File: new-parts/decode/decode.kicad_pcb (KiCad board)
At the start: 2 copper layers, 96.5 x 82.5 mm, 45 parts, among them J1 BHR-10-VUA, J10 Conn_02x01, J11 Conn_02x01, J12 Conn_02x01, J13 Conn_02x01, J14 Conn_02x01, J2 Conn_02x01, J3 Conn_02x01, J4 Conn_02x01, J5 Conn_02x01, J6 Conn_02x03_Odd_Even, J7 Conn_02x01, J8 Conn_02x01, J9 Conn_02x01, K1 J104D2C12VDC.15S, K2 J104D2C12VDC.15S, K3 J104D2C12VDC.15S, K4 J104D2C12VDC.15S, K5 J104D2C12VDC.15S, K6 J104D2C12VDC.15S, K7 J104D2C12VDC.15S, K8 J104D2C12VDC.15S, K9 J104D2C12VDC.15S

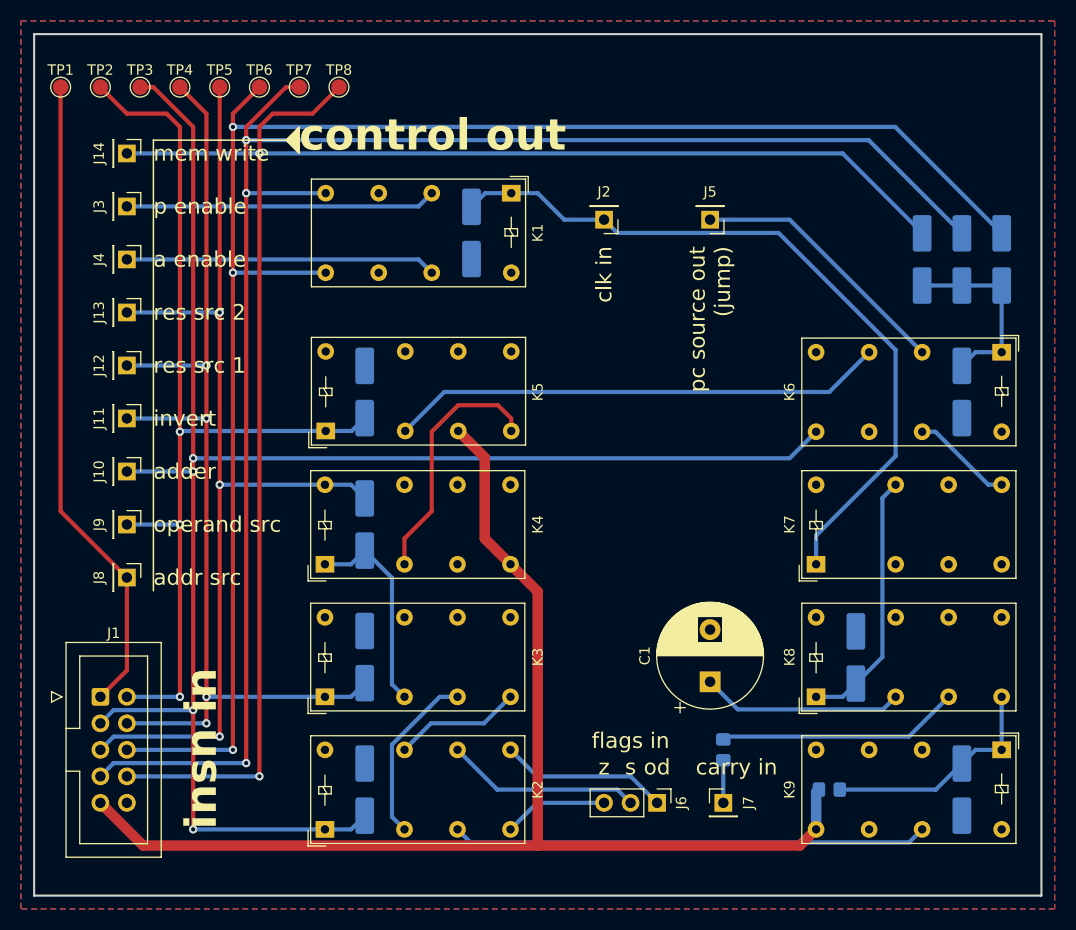
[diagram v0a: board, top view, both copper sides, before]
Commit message: decode: Also provide !invert control signal as carry in for the adder, provide 4 pins for every control signal.
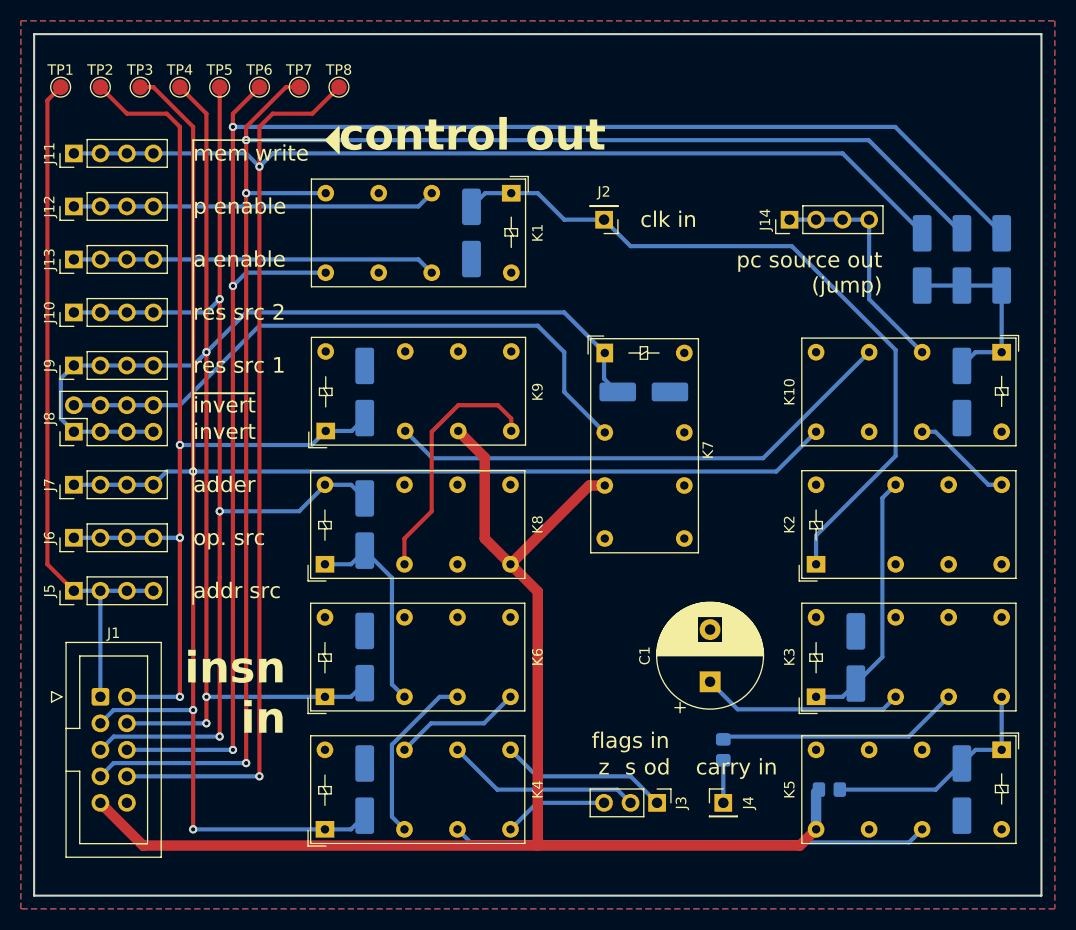
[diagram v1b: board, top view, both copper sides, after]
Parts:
- removed the J3 at (142.2, 43.2)
- removed the J4 at (142.2, 48.3)
- added D6: SMAJ14CA, Diode_SMD:D_SMA_Handsoldering, B.Cu at (191.8, 61.0)
- added J6: Conn_01x04, Connector_PinHeader_2.54mm:PinHeader_1x04_P2.54mm_Vertical, F.Cu at (137.2, 74.9)
- added J7: Conn_01x04, Connector_PinHeader_2.54mm:PinHeader_1x04_P2.54mm_Vertical, F.Cu at (137.2, 69.8)
- added K7: J104D2C12VDC.15S, Relay_THT:Relay_DPDT_Finder_30.22, F.Cu at (188.0, 57.2)
- J10, J11, J12, J13, J14, J5, J9: value Conn_02x01 -> Conn_01x04; footprint Connector_PinHeader_2.54mm:PinHeader_1x01_P2.54mm_Vertical -> Connector_PinHeader_2.54mm:PinHeader_1x04_P2.54mm_Vertical
- J2: value Conn_02x01 -> Conn_01x01
- J3: renamed from J6; value Conn_02x03_Odd_Even -> Conn_01x03
- J4: renamed from J7; value Conn_02x01 -> Conn_01x01
- J8: value Conn_02x01 -> Conn_02x04_Odd_Even; footprint Connector_PinHeader_2.54mm:PinHeader_1x01_P2.54mm_Vertical -> Connector_PinHeader_2.54mm:PinHeader_2x04_P2.54mm_Vertical
- moved J5 70.6 mm to (137.2, 80.0), turned to 90 degrees
- moved J14 63.8 mm to (205.7, 44.5), turned to 90 degrees
- moved J11 25.9 mm to (137.2, 38.1), turned to 90 degrees
- moved J12 16.1 mm to (137.2, 43.2), turned to 90 degrees
- moved J10 16.1 mm to (137.2, 53.3), turned to 90 degrees
- moved J9 16.1 mm to (137.2, 58.4), turned to 90 degrees
- moved J8 14.9 mm to (137.2, 64.8), turned to 90 degrees
- moved J13 7.18 mm to (137.2, 48.3), turned to 90 degrees
- renumbered D8 to D10, D9 to D11, D6 to D12, D11 to D2, D2 to D3, D12 to D4, D3 to D5, D4 to D7, D5 to D8, D7 to D9, K6 to K10, K7 to K2, K8 to K3, K2 to K4, K9 to K5, K3 to K6, K4 to K8, K5 to K9
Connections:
- J10 pad 1: add -> cinv
- J11 pad 1: c2 -> m en
- J12 pad 1: c2 -> /p en out
- J13 pad 1: cinv -> /a en out
- J14 pad 1: m en -> /pc src out
- J5 pad 1: /pc src out -> as
- J8 pad 1: as -> c2
- J9 pad 1: cond -> c2
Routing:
- net ~{inv}: track 0.00 -> 60.5 mm
- net c2: track 100.6 -> 159.3 mm, vias 4 -> 3
- net VCC: track 117.7 -> 129.9 mm
- net cinv: track 97.5 -> 104.2 mm
- net m en: track 163.5 -> 169.7 mm
- net add: track 167.5 -> 173.6 mm, vias 4 -> 3
- net cond: track 92.2 -> 97.8 mm
- net as: track 62.1 -> 67.6 mm
- net /p en out: track 29.7 -> 34.8 mm
- net /a en out: track 29.7 -> 34.8 mm
- net /pc src out: track 25.6 -> 22.4 mm
- net Net-(K10-Pad12): track 47.6 -> 49.7 mm
- net a en: track 161.5 -> 162.0 mm
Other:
- board text added: "op. src"
- board text added: "~{invert}"
- board text removed: "operand src"

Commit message: Add signatures to some boards.
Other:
- board text added: "github.com/fread/visvitalis"
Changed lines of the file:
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@@
 		(tags "Through hole pin header THT 1x04 2.54mm single row")
 		(property "Reference" "J13"
-			(at 0 -2.33 270)
+			(at 0 -2.33 -90)
 			(layer "F.SilkS")
 			(effects
@@
 		)
 		(property "Value" "Conn_01x04"
-			(at 0 9.95 270)
+			(at 0 9.95 -90)
 			(layer "F.Fab")
 			(effects
@@
 		)
 		(fp_text user "${REFERENCE}"
-			(at 0 3.81 360)
+			(at 0 3.81 0)
 			(layer "F.Fab")
 			(effects
@@
 		(tags "Through hole pin header THT 1x04 2.54mm single row")
 		(property "Reference" "J10"
-			(at 0 -2.33 270)
+			(at 0 -2.33 -90)
 			(layer "F.SilkS")
 			(effects
@@
 		)
 		(property "Value" "Conn_01x04"
-			(at 0 9.95 270)
+			(at 0 9.95 -90)
 			(layer "F.Fab")
 			(effects
@@
 		)
 		(fp_text user "${REFERENCE}"
-			(at 0 3.81 360)
+			(at 0 3.81 0)
 			(layer "F.Fab")
 			(effects
@@
 		(tags "Through hole pin header THT 1x04 2.54mm single row")
 		(property "Reference" "J5"
-			(at 0 -2.33 270)
+			(at 0 -2.33 -90)
 			(layer "F.SilkS")
 			(effects
@@
 		)
 		(property "Value" "Conn_01x04"
-			(at 0 9.95 270)
+			(at 0 9.95 -90)
 			(layer "F.Fab")
 			(effects
@@
 		)
 		(fp_text user "${REFERENCE}"
-			(at 0 3.81 360)
+			(at 0 3.81 0)
 			(layer "F.Fab")
 			(effects
@@
 		(tags "Through hole pin header THT 1x04 2.54mm single row")
 		(property "Reference" "J6"
-			(at 0 -2.33 270)
+			(at 0 -2.33 -90)
 			(layer "F.SilkS")
 			(effects
@@
 		)
 		(property "Value" "Conn_01x04"
-			(at 0 9.95 270)
+			(at 0 9.95 -90)
 			(layer "F.Fab")
 			(effects
@@
 		)
 		(fp_text user "${REFERENCE}"
-			(at 0 3.81 360)
+			(at 0 3.81 0)
 			(layer "F.Fab")
 			(effects
@@
 		(tags "Through hole pin header THT 2x04 2.54mm double row")
 		(property "Reference" "J8"
-			(at 1.27 -2.33 270)
+			(at 1.27 -2.33 -90)
 			(layer "F.SilkS")
 			(effects
@@
 		)
 		(property "Value" "Conn_02x04_Odd_Even"
-			(at 1.27 9.95 270)
+			(at 1.27 9.95 -90)
 			(layer "F.Fab")
 			(effects
@@
 		)
 		(fp_text user "${REFERENCE}"
-			(at 1.27 3.81 360)
+			(at 1.27 3.81 0)
 			(layer "F.Fab")
 			(effects
@@
 		(tags "Through hole pin header THT 1x04 2.54mm single row")
 		(property "Reference" "J7"
-			(at 0 -2.33 270)
+			(at 0 -2.33 -90)
 			(layer "F.SilkS")
 			(effects
@@
 		)
 		(property "Value" "Conn_01x04"
-			(at 0 9.95 270)
+			(at 0 9.95 -90)
 			(layer "F.Fab")
 			(effects
@@
 		)
 		(fp_text user "${REFERENCE}"
-			(at 0 3.81 360)
+			(at 0 3.81 0)
 			(layer "F.Fab")
 			(effects
@@
 		(tags "Through hole pin header THT 1x04 2.54mm single row")
 		(property "Reference" "J14"
-			(at 0 -2.33 270)
+			(at 0 -2.33 -90)
 			(layer "F.SilkS")
 			(effects
@@
 		)
 		(property "Value" "Conn_01x04"
-			(at 0 9.95 270)
+			(at 0 9.95 -90)
 			(layer "F.Fab")
 			(effects
@@
 		)
 		(fp_text user "${REFERENCE}"
-			(at 0 3.81 360)
+			(at 0 3.81 0)
 			(layer "F.Fab")
 			(effects
@@
 		(tags "Through hole pin header THT 1x04 2.54mm single row")
 		(property "Reference" "J11"
-			(at 0 -2.33 270)
+			(at 0 -2.33 -90)
 			(layer "F.SilkS")
 			(effects
@@
 		)
 		(property "Value" "Conn_01x04"
-			(at 0 9.95 270)
+			(at 0 9.95 -90)
 			(layer "F.Fab")
 			(effects
@@
 		)
 		(fp_text user "${REFERENCE}"
-			(at 0 3.81 360)
+			(at 0 3.81 0)
 			(layer "F.Fab")
 			(effects
@@
 		(tags "Through hole pin header THT 1x04 2.54mm single row")
 		(property "Reference" "J9"
-			(at 0 -2.33 270)
+			(at 0 -2.33 -90)
 			(layer "F.SilkS")
 			(effects
@@
 		)
 		(property "Value" "Conn_01x04"
-			(at 0 9.95 270)
+			(at 0 9.95 -90)
 			(layer "F.Fab")
 			(effects
@@
 		)
 		(fp_text user "${REFERENCE}"
-			(at 0 3.81 360)
+			(at 0 3.81 0)
 			(layer "F.Fab")
 			(effects
@@
 		(tags "Through hole pin header THT 1x04 2.54mm single row")
 		(property "Reference" "J12"
-			(at 0 -2.33 270)
+			(at 0 -2.33 -90)
 			(layer "F.SilkS")
 			(effects
@@
 		)
 		(property "Value" "Conn_01x04"
-			(at 0 9.95 270)
+			(at 0 9.95 -90)
 			(layer "F.Fab")
 			(effects
@@
 		)
 		(fp_text user "${REFERENCE}"
-			(at 0 3.81 360)
+			(at 0 3.81 0)
 			(layer "F.Fab")
 			(effects
@@
 		)
 	)
+	(gr_poly
+		(pts
+			(xy 136.868649 104.954117) (xy 134.714081 104.954117) (xy 134.714081 105.79543) (xy 136.273758 105.79543)
+			(xy 134.912175 107.157002) (xy 135.507078 107.751905) (xy 136.868651 106.390315) (xy 136.868651 107.95)
+			(xy 137.709953 107.95) (xy 137.709953 105.795431) (xy 139.864483 105.795431) (xy 139.864483 104.954118)
+			(xy 138.304828 104.954118) (xy 138.780865 104.478077) (xy 138.879962 104.383834) (xy 138.982531 104.29567)
+			(xy 139.08834 104.213587) (xy 139.197158 104.137584) (xy 139.308753 104.067661) (xy 139.422894 104.003818)
+			(xy 139.53935 103.946056) (xy 139.657888 103.894374) (xy 139.778279 103.848772) (xy 139.900289 103.809251)
+			(xy 140.023688 103.775809) (xy 140.148244 103.748448) (xy 140.273726 103.727167) (xy 140.399903 103.711967)
+			(xy 140.526542 103.702846) (xy 140.653413 103.699806) (xy 140.780283 103.702846) (xy 140.906923 103.711967)
+			(xy 141.033099 103.727167) (xy 141.158581 103.748448) (xy 141.283137 103.775809) (xy 141.406536 103.809251)
+			(xy 141.528547 103.848772) (xy 141.648937 103.894374) (xy 141.767476 103.946056) (xy 141.883931 104.003818)
+			(xy 141.998072 104.067661) (xy 142.109667 104.137584) (xy 142.218485 104.213587) (xy 142.324294 104.29567)
+			(xy 142.426863 104.383834) (xy 142.52596 104.478077) (xy 143.002 104.954118) (xy 141.442343 104.954118)
+			(xy 141.442343 105.795431) (xy 143.596873 105.795431) (xy 143.596873 107.95) (xy 144.438176 107.95)
+			(xy 144.438176 106.390295) (xy 145.799786 107.751905) (xy 146.39465 107.157003) (xy 145.033087 105.795431)
+			(xy 146.592744 105.795431) (xy 146.592744 104.954118) (xy 144.438176 104.954118) (xy 144.438176 102.799588)
+			(xy 143.596872 102.799586) (xy 143.596872 104.359215) (xy 143.12086 103.883205) (xy 142.990976 103.759761)
+			(xy 142.856383 103.644282) (xy 142.717395 103.536766) (xy 142.574325 103.437213) (xy 142.427488 103.345624)
+			(xy 142.277198 103.261999) (xy 142.123769 103.186338) (xy 141.967514 103.11864) (xy 141.808747 103.058907)
+			(xy 141.647783 103.007138) (xy 141.484936 102.963333) (xy 141.320518 102.927493) (xy 141.154845 102.899617)
+			(xy 140.98823 102.879705) (xy 140.820988 102.867758) (xy 140.653431 102.863776) (xy 140.485875 102.867758)
+			(xy 140.318632 102.879705) (xy 140.152017 102.899617) (xy 139.986344 102.927493) (xy 139.821927 102.963333)
+			(xy 139.659079 103.007138) (xy 139.498115 103.058907) (xy 139.339348 103.11864) (xy 139.183093 103.186338)
+			(xy 139.029664 103.261999) (xy 138.879373 103.345624) (xy 138.732536 103.437213) (xy 138.589467 103.536766)
+			(xy 138.450479 103.644282) (xy 138.315885 103.759761) (xy 138.186001 103.883205) (xy 137.709952 104.359254)
+			(xy 137.709952 102.799586) (xy 136.868649 102.799586)
+		)
+		(stroke
+			(width -0.000001)
+			(type solid)
+		)
+		(fill solid)
+		(layer "B.SilkS")
+	)
 	(gr_line
 		(start 148.59 81.28)
@@
 		)
 	)
+	(gr_text "github.com/fread/visvitalis"
+		(at 147.574 106.934 0)
+		(layer "B.SilkS")
+		(effects
+			(font
+				(size 1.5 1.5)
+				(thickness 0.3)
+				(bold yes)
+			)
+			(justify right mirror)
+		)
+	)
 	(gr_text "res src 2"
 		(at 148.59 53.34 0)
@@
 		)
 	)
+	(group ""
+		(members "4d71ad70-9a42-49ae-8040-978068f2cbaa")
+	)
 )
